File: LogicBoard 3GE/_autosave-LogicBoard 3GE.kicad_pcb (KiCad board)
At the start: 4 copper layers, 103.1 x 140.1 mm, 167 parts, among them IC103 LM386-3, IC201 27C512PLCC, IC202 74LS00, IC203 74LS32, IC204 CY62256-70PC, IC206 68A09, IC207 6522, IC208 AY3-8912, IC301 DAC0808LCMX/NOPB, IC302 CD4052B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

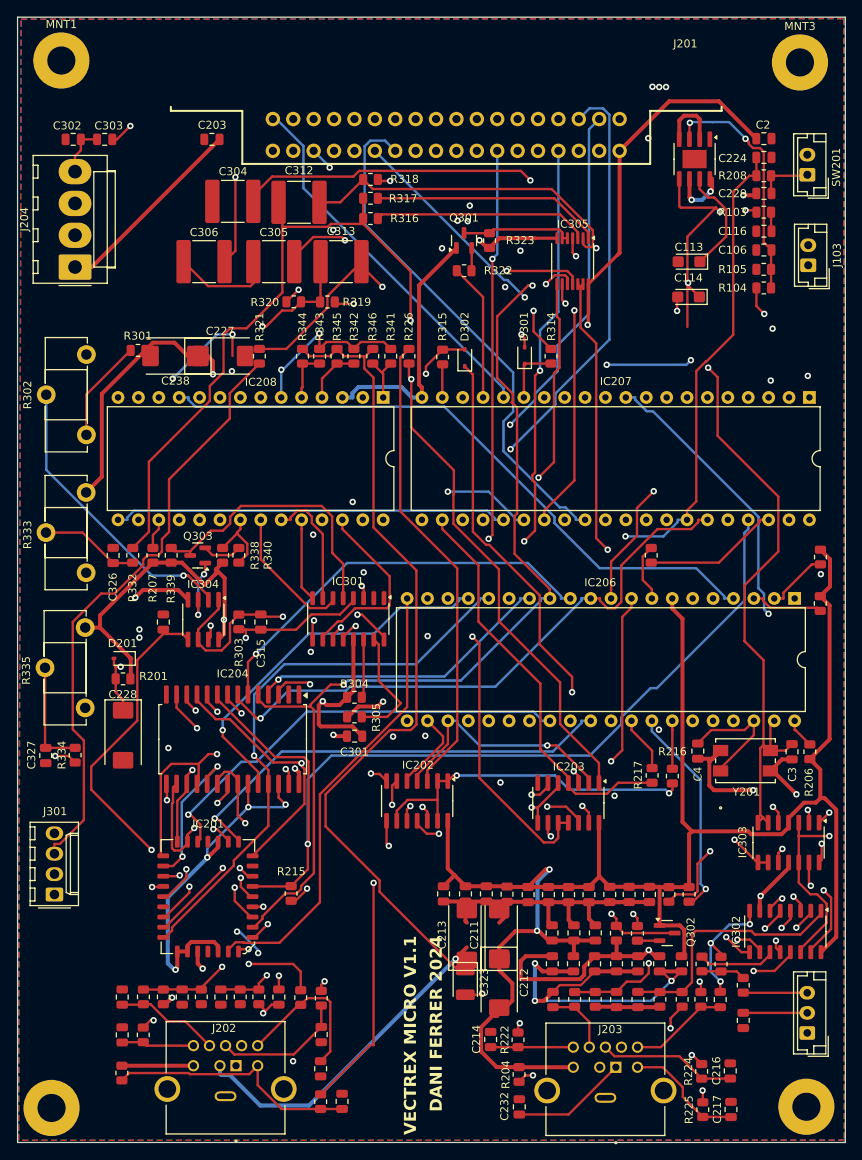
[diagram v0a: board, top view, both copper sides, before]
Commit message: changed packages and symbols to fit Mouser BOM
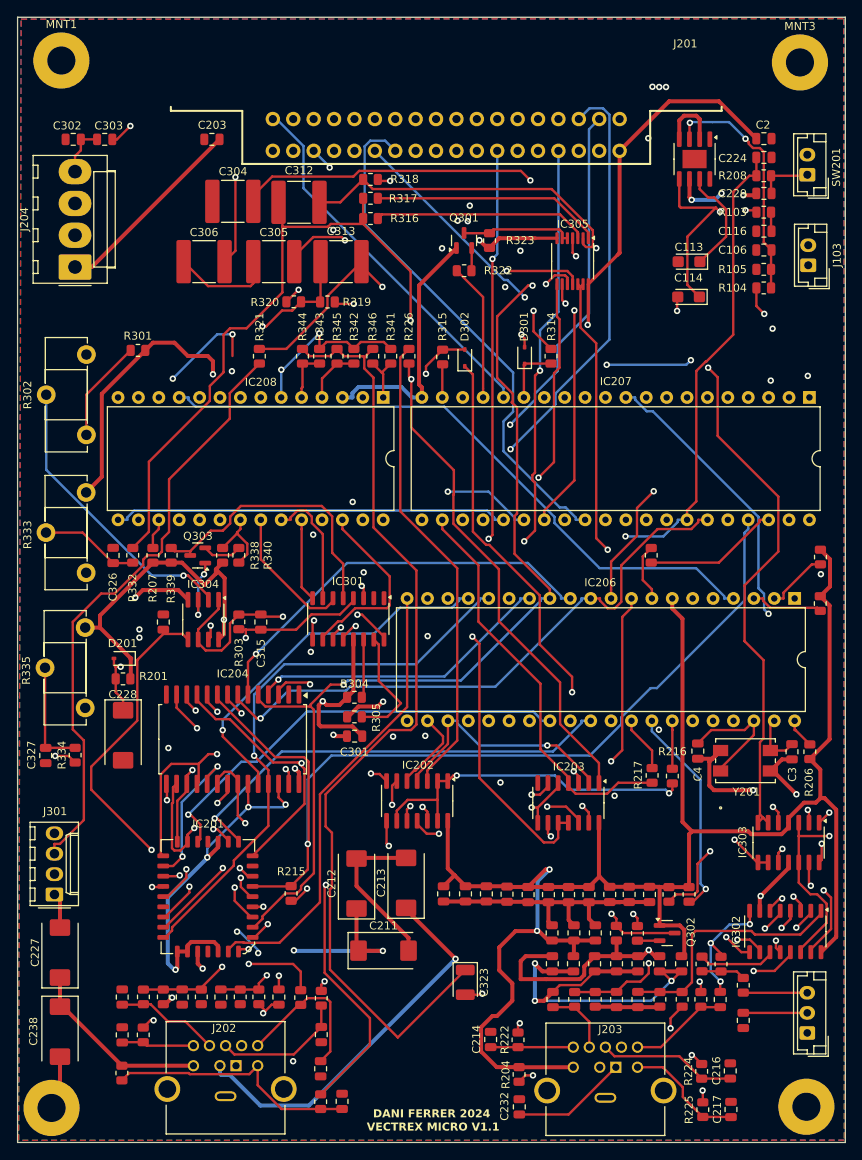
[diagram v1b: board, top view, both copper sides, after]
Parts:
- moved C238 85.4 mm to (53.6, 153.5), turned to -90 degrees
- moved C227 76.9 mm to (53.6, 143.7), turned to 90 degrees
- moved C212 21.6 mm to (90.5, 135.1), turned to 90 degrees
- moved C211 14.5 mm to (93.9, 143.4), turned to 0 degrees
- moved C213 9.97 mm to (96.7, 135.0)
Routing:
- net +5V: track 640.7 -> 675.8 mm, vias 11 -> 13
- net GND: track 306.3 -> 332.2 mm
- net /CH(A+B+C): track 103.3 -> 119.8 mm
- net /SW7: track 195.6 -> 203.3 mm
- net -5VA: track 364.0 -> 370.9 mm
- net Net-(C114-Pad1): track 32.1 -> 26.7 mm, vias 3 -> 2
